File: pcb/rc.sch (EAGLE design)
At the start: 67 parts, among them IC2 TP4056

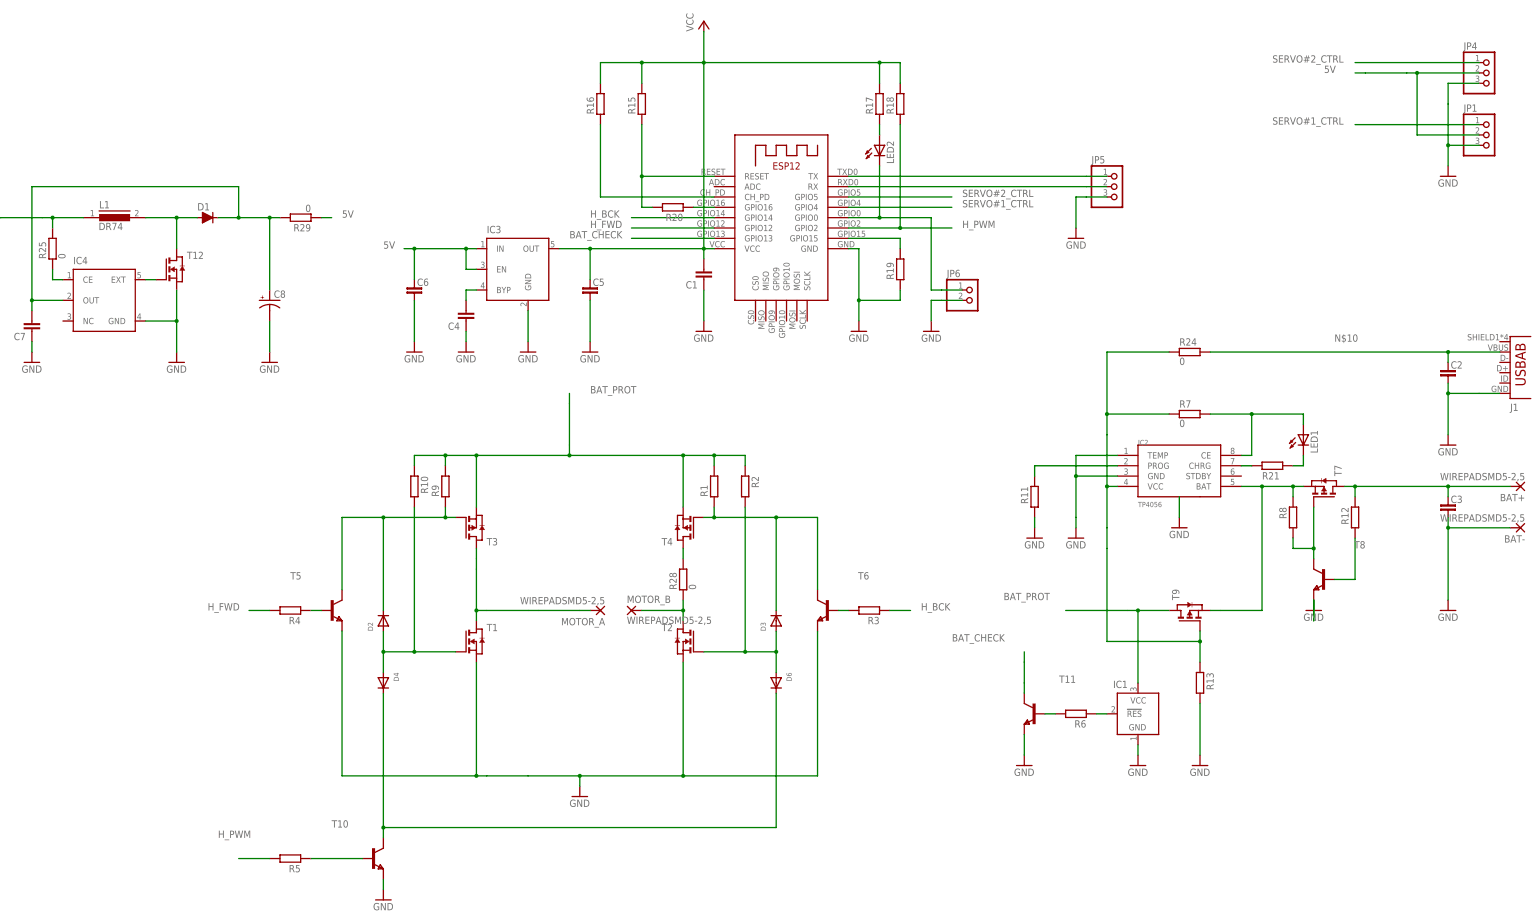
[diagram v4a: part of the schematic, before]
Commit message: add values for some components
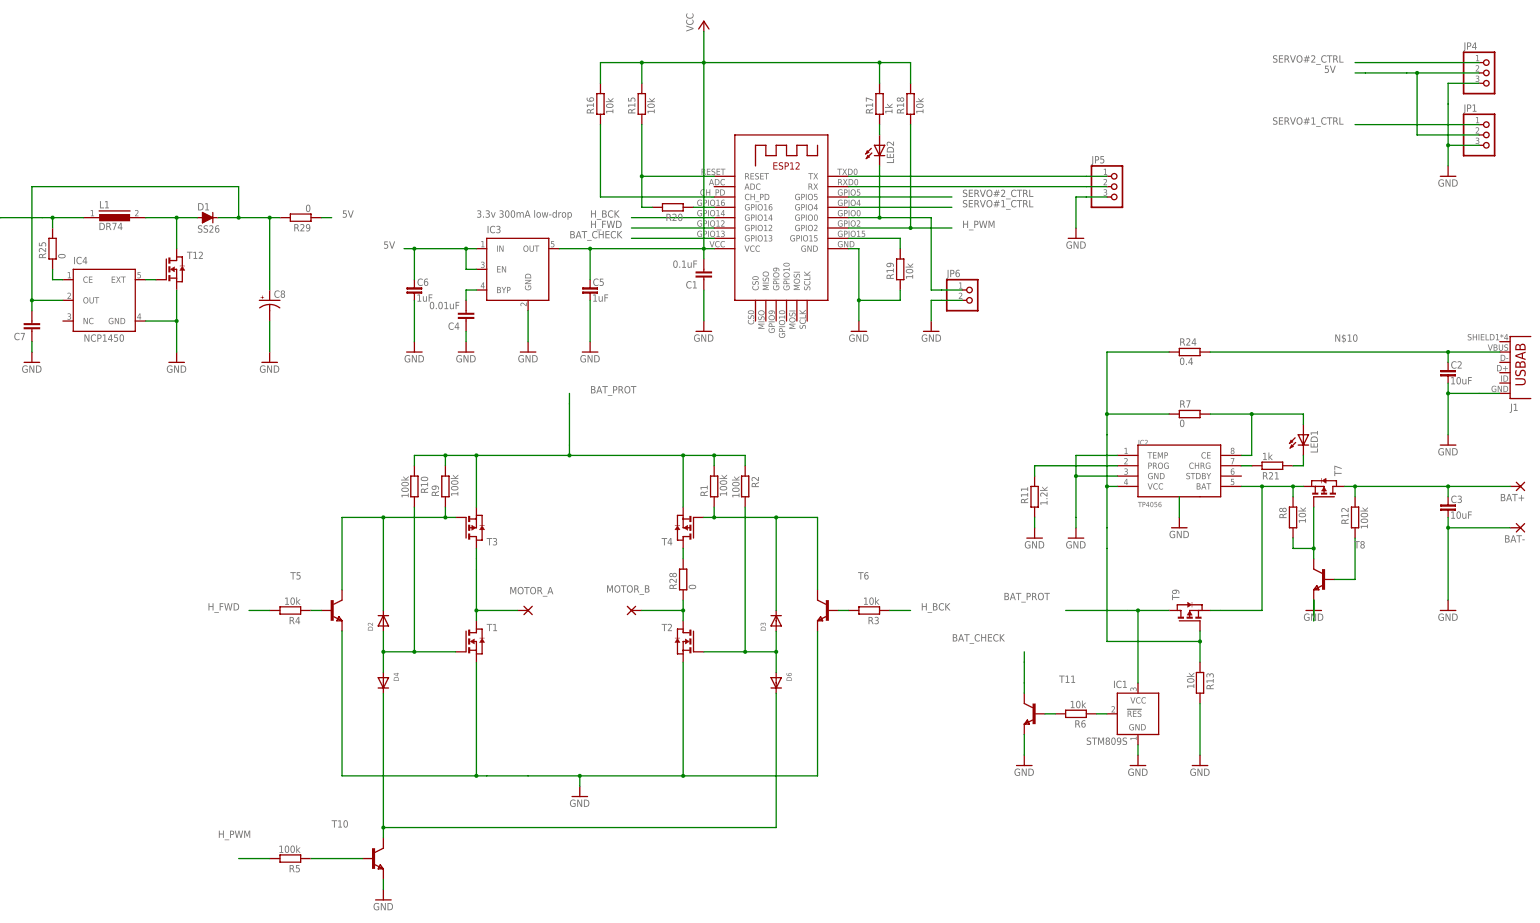
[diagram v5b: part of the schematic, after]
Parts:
- C1: value (none) -> 0.1uF
- C2, C3: value (none) -> 10uF
- C4: value (none) -> 0.01uF
- C5, C6: value (none) -> 1uF
- D1: value (none) -> SS26
- IC1: value (none) -> STM809S
- IC3: value (none) -> 3.3v 300mA low-drop
- IC4: value (none) -> NCP1450
- R1, R10, R12, R2, R5, R9: value (none) -> 100k
- R11: value (none) -> 1.2k
- R13, R15, R16, R18, R19, R3, R4, R6, R8: value (none) -> 10k
- R17, R21: value (none) -> 1k
- R24: value 0 -> 0.4
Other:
- moved on the sheet: MOTOR_A, R18
